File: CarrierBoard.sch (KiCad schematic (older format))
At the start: 14 parts, among them U10 PowerStage_L

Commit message: add files
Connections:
- net labels added: 5V_IN_RAW
- wire segments 21 -> 19
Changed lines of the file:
@@
 	9600 3150 9600 3220
 Connection ~ 9600 3220
-Wire Wire Line
-	7350 2520 7350 2530
 Text HLabel 7350 2820 2    50   Input ~ 0
 5V
@@
 	1    8700 2000
 	1    0    0    -1
-$EndComp
-Wire Wire Line
-	7330 2530 7350 2530
-Connection ~ 7350 2530
-Wire Wire Line
-	7350 2530 7350 2820
-$Comp
-L Device:D_Schottky D?
-U 1 1 6167ACF2
-P 7350 2380
-AR Path="/60F72524/6167ACF2" Ref="D?"  Part="1"
-AR Path="/61662381/6167ACF2" Ref="D2"  Part="1"
-F 0 "D2" V 7396 2301 50  0000 R CNN
-F 1 "D_Schottky" V 7305 2301 50  0000 R CNN
-F 2 "Diode_SMD:D_0603_1608Metric_Pad1.05x0.95mm_HandSolder" H 7350 2380 50  0001 C CNN
-F 3 "~" H 7350 2380 50  0001 C CNN
-	1    7350 2380
-	0    -1   -1   0
 $EndComp
 Wire Wire Line
@@
 Wire Wire Line
 	7350 2000 7350 2230
+$Comp
+L Device:D_Schottky D?
+U 1 1 6167ACF2
+P 7350 2380
+AR Path="/60F72524/6167ACF2" Ref="D?"  Part="1"
+AR Path="/61662381/6167ACF2" Ref="D2"  Part="1"
+F 0 "D2" V 7396 2301 50  0000 R CNN
+F 1 "D_Schottky" V 7305 2301 50  0000 R CNN
+F 2 "Diode_SMD:D_0603_1608Metric_Pad1.05x0.95mm_HandSolder" H 7350 2380 50  0001 C CNN
+F 3 "~" H 7350 2380 50  0001 C CNN
+	1    7350 2380
+	0    -1   -1   0
+$EndComp
+Wire Wire Line
+	7350 2530 7350 2820
+Text Label 7330 1220 0    50   ~ 0
+5V_IN_RAW
+Text Label 4400 2950 2    50   ~ 0
+5V_IN_RAW
 $EndSCHEMATC

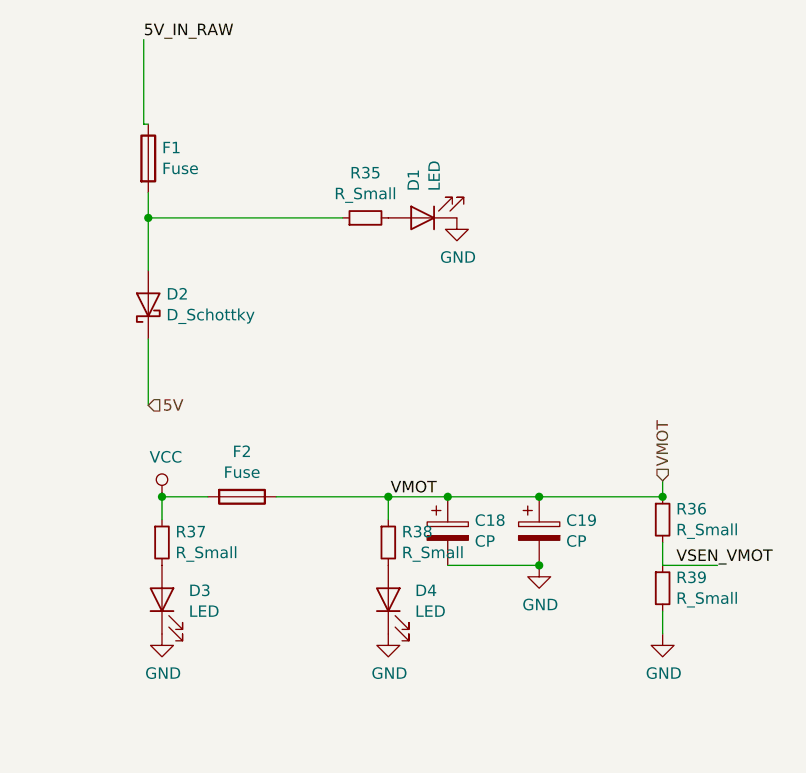
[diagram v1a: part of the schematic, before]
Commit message: update passive components values
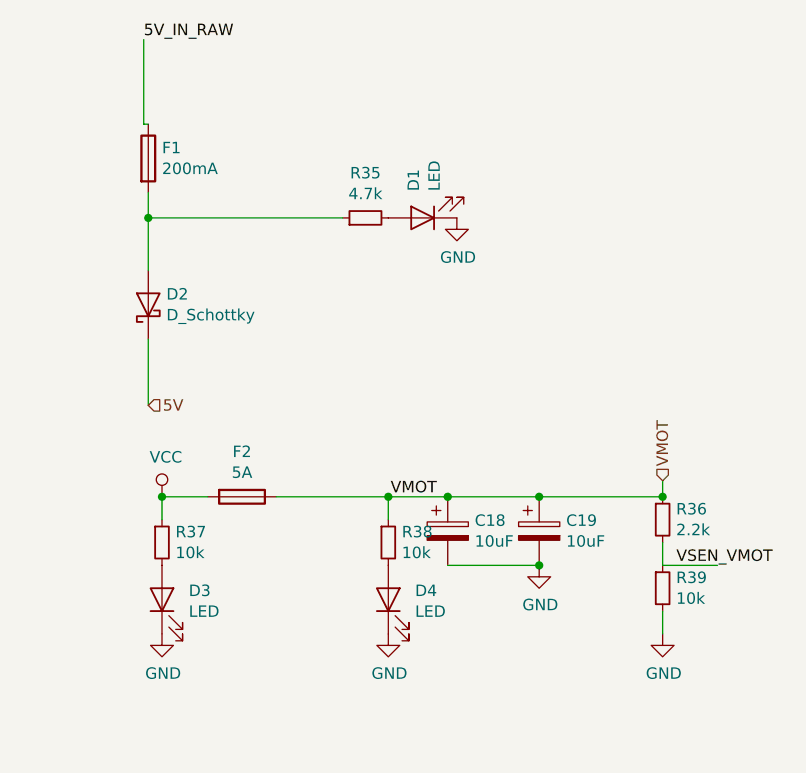
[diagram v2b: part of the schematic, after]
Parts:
- C18, C19: value CP -> 10uF
- F1: value Fuse -> 200mA
- F2: value Fuse -> 5A
- R35: value R_Small -> 4.7k
- R36: value R_Small -> 2.2k
- R37, R38, R39: value R_Small -> 10k
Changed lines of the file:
@@
 AR Path="/61662381/6166F077" Ref="F2"  Part="1"
 F 0 "F2" V 7563 3220 50  0000 C CNN
-F 1 "Fuse" V 7654 3220 50  0000 C CNN
+F 1 "5A" V 7654 3220 50  0000 C CNN
 F 2 "Fuse:Fuse_1210_3225Metric_Pad1.42x2.65mm_HandSolder" V 7690 3220 50  0001 C CNN
 F 3 "~" H 7760 3220 50  0001 C CNN
@@
 AR Path="/61662381/6166F08A" Ref="C18"  Part="1"
 F 0 "C18" H 8778 3416 50  0000 L CNN
-F 1 "CP" H 8778 3325 50  0000 L CNN
+F 1 "10uF" H 8778 3325 50  0000 L CNN
 F 2 "Capacitor_THT:CP_Radial_D10.0mm_P5.00mm" H 8698 3220 50  0001 C CNN
 F 3 "~" H 8660 3370 50  0001 C CNN
@@
 AR Path="/61662381/6166F090" Ref="C19"  Part="1"
 F 0 "C19" H 9178 3416 50  0000 L CNN
-F 1 "CP" H 9178 3325 50  0000 L CNN
+F 1 "10uF" H 9178 3325 50  0000 L CNN
 F 2 "Capacitor_THT:CP_Radial_D10.0mm_P5.00mm" H 9098 3220 50  0001 C CNN
 F 3 "~" H 9060 3370 50  0001 C CNN
@@
 AR Path="/61662381/6166F0BD" Ref="R38"  Part="1"
 F 0 "R38" H 8459 3466 50  0000 L CNN
-F 1 "R_Small" H 8459 3375 50  0000 L CNN
+F 1 "10k" H 8459 3375 50  0000 L CNN
 F 2 "Resistor_SMD:R_0402_1005Metric" H 8400 3420 50  0001 C CNN
 F 3 "~" H 8400 3420 50  0001 C CNN
@@
 AR Path="/61662381/6166F0C3" Ref="R36"  Part="1"
 F 0 "R36" H 9659 3366 50  0000 L CNN
-F 1 "R_Small" H 9659 3275 50  0000 L CNN
+F 1 "2.2k" H 9659 3275 50  0000 L CNN
 F 2 "Resistor_SMD:R_0402_1005Metric" H 9600 3320 50  0001 C CNN
 F 3 "~" H 9600 3320 50  0001 C CNN
@@
 AR Path="/61662381/6166F0C9" Ref="R39"  Part="1"
 F 0 "R39" H 9659 3666 50  0000 L CNN
-F 1 "R_Small" H 9659 3575 50  0000 L CNN
+F 1 "10k" H 9659 3575 50  0000 L CNN
 F 2 "Resistor_SMD:R_0402_1005Metric" H 9600 3620 50  0001 C CNN
 F 3 "~" H 9600 3620 50  0001 C CNN
@@
 AR Path="/61662381/6166F0CF" Ref="R37"  Part="1"
 F 0 "R37" H 7469 3466 50  0000 L CNN
-F 1 "R_Small" H 7469 3375 50  0000 L CNN
+F 1 "10k" H 7469 3375 50  0000 L CNN
 F 2 "Resistor_SMD:R_0402_1005Metric" H 7410 3420 50  0001 C CNN
 F 3 "~" H 7410 3420 50  0001 C CNN
@@
 AR Path="/61662381/6167ACE2" Ref="F1"  Part="1"
 F 0 "F1" H 7410 1786 50  0000 L CNN
-F 1 "Fuse" H 7410 1695 50  0000 L CNN
+F 1 "200mA" H 7410 1695 50  0000 L CNN
 F 2 "Fuse:Fuse_0603_1608Metric_Pad1.05x0.95mm_HandSolder" V 7280 1740 50  0001 C CNN
 F 3 "~" H 7350 1740 50  0001 C CNN
@@
 AR Path="/61662381/6167ACFA" Ref="R35"  Part="1"
 F 0 "R35" V 8496 2000 50  0000 C CNN
-F 1 "R_Small" V 8405 2000 50  0000 C CNN
+F 1 "4.7k" V 8405 2000 50  0000 C CNN
 F 2 "Resistor_SMD:R_0402_1005Metric" H 8300 2000 50  0001 C CNN
 F 3 "~" H 8300 2000 50  0001 C CNN
